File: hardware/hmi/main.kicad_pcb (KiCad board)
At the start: 2 copper layers, 80 x 80 mm, 54 parts, among them J1 LOAD_CON, J2 Conn_01x08, J3 SD_CARD, J4 ENCODER, SW1 CC, SW2 CV, SW3 CR, SW4 CP, SW5 EN, U1 ESP32-DEVKIT-V1

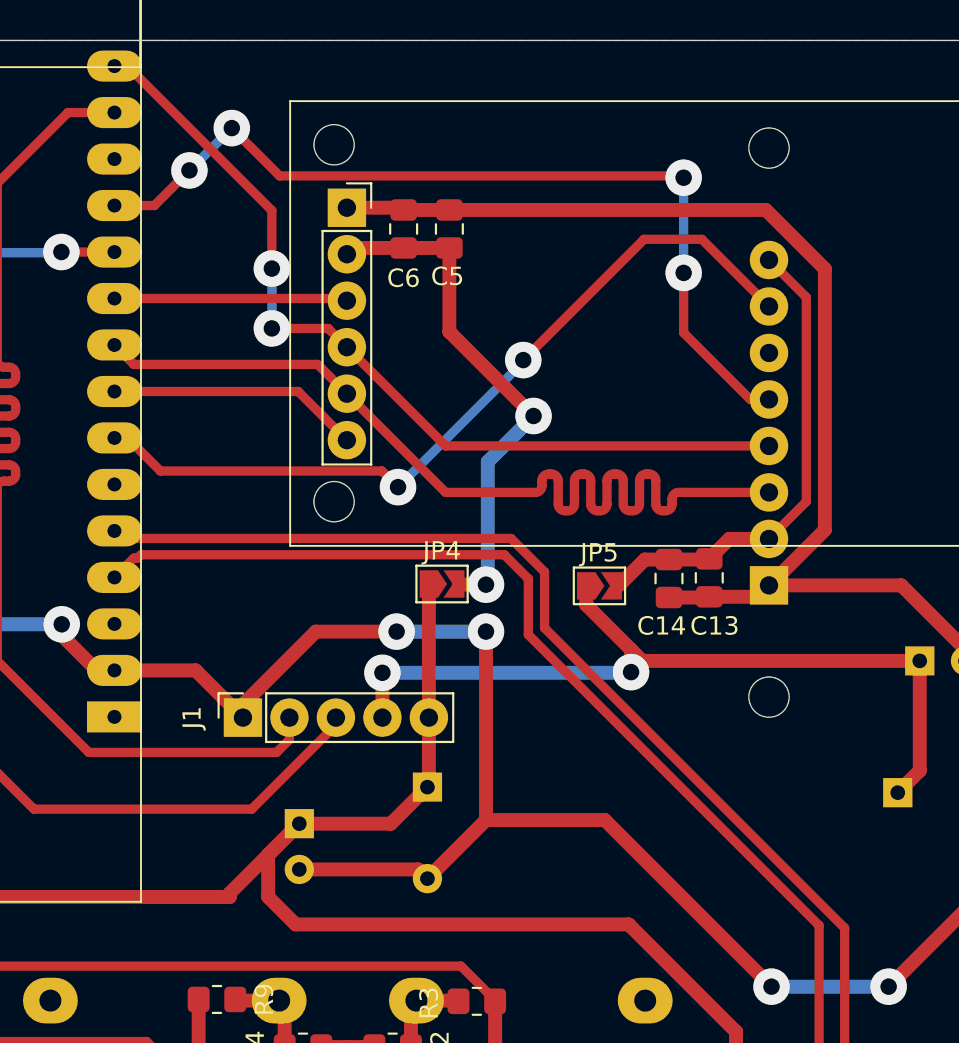
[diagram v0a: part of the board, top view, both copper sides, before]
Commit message: fix: conect DC pin and change reset to avoid conflicts with UART
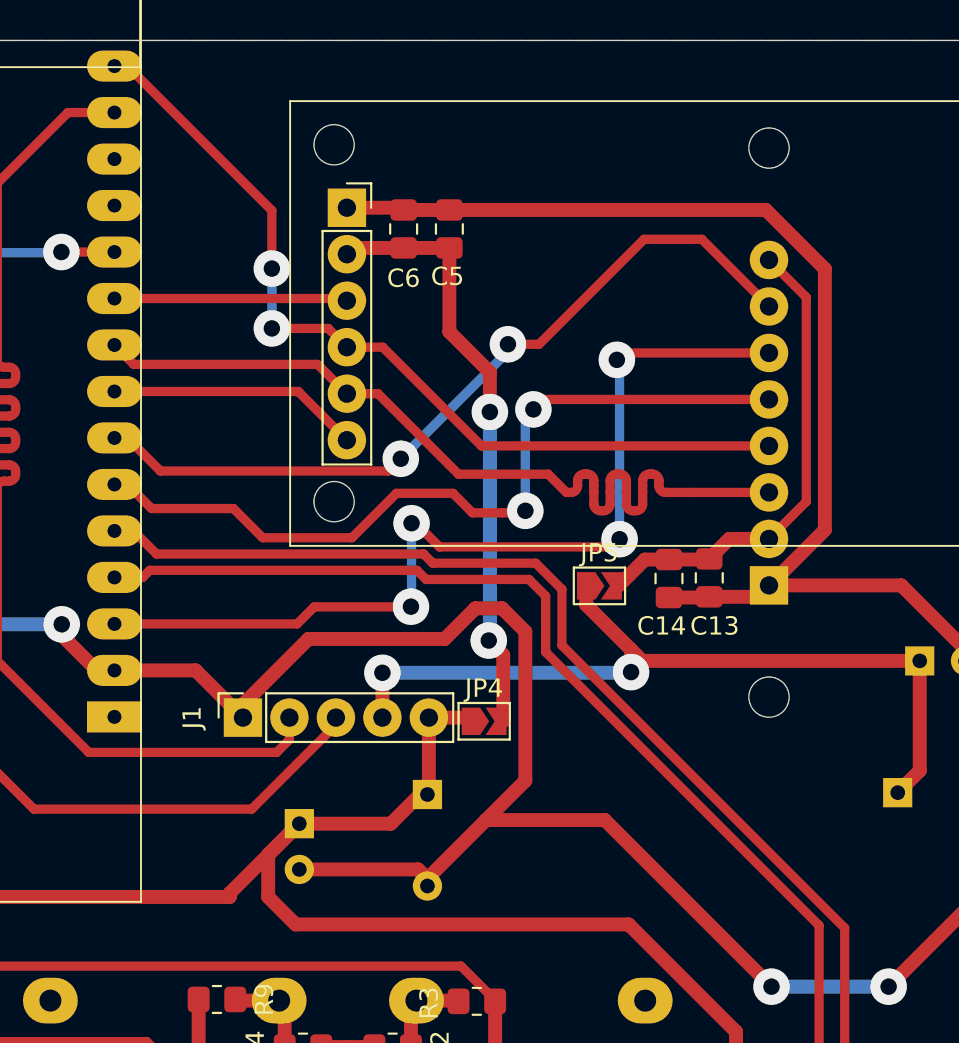
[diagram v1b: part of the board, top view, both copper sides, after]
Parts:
- moved JP4 7.84 mm to (122.5, 96.0)
- moved C1 0.40 mm to (119.4, 100.0)
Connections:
- J2 pad 6: unconnected-(J2-Pin_6-Pad6) -> /DISPLAY/DC
- U1 pad 12: /DISPLAY/RST -> unconnected-(U1-GPIO_3/RX0-Pad12)
- U1 pad 3: unconnected-(U1-GPIO_15_/ADC_13-Pad3) -> /DISPLAY/DC
- U1 pad 6: unconnected-(U1-GPIO_16/RX2-Pad6) -> /DISPLAY/RST
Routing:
- net /DISPLAY/DC: track 0.00 -> 51.6 mm, vias 0 -> 4
- net /DISPLAY/SCK: track 52.1 -> 47.1 mm
- net +5V: track 137.6 -> 132.7 mm
- net /DISPLAY/RST: track 48.6 -> 44.0 mm, vias 4 -> 2
- net Net-(J3-Pin_2): track 28.5 -> 32.9 mm
- net GND: track 377.3 -> 381.4 mm, vias 9 -> 7
- net /ESP32/BTN_EN: track 77.5 -> 76.8 mm
- net /DISPLAY/CS: track 44.1 -> 43.5 mm

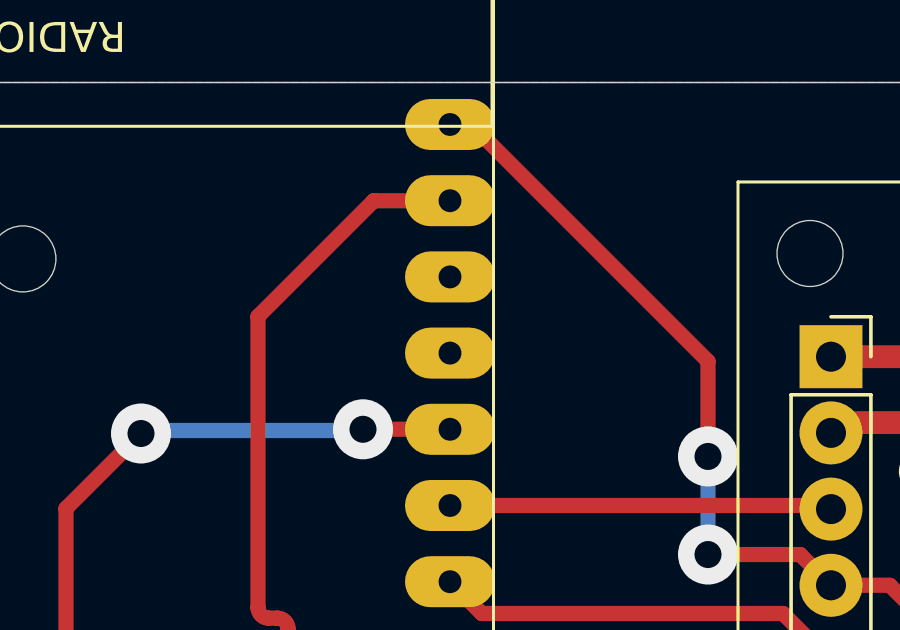
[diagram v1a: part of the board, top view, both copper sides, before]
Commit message: hardware: hmi: Change to UART
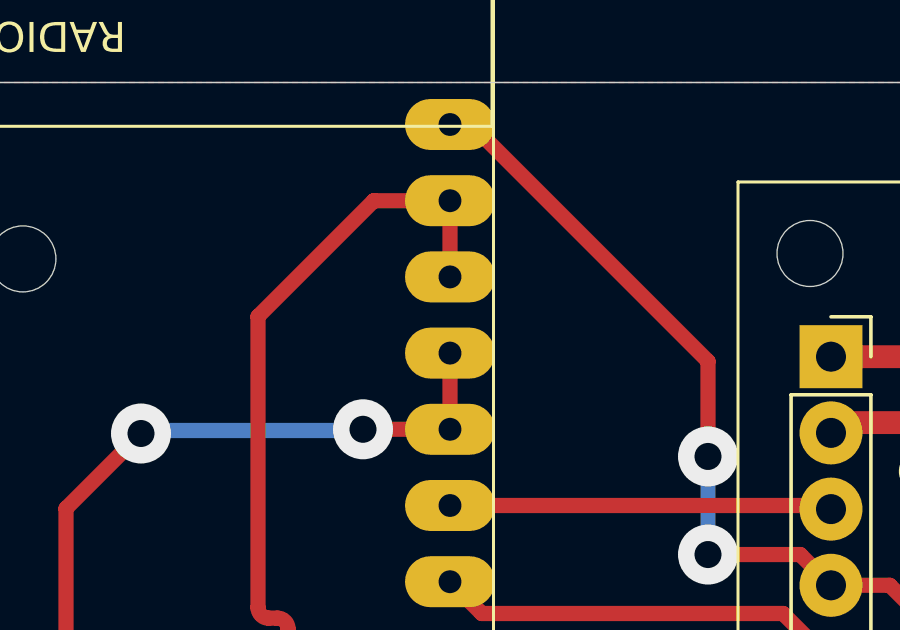
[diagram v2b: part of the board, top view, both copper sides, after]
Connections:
- U1 pad 12: unconnected-(U1-GPIO_3/RX0-Pad12) -> /LOAD_SCL
- U1 pad 13: unconnected-(U1-GPIO_1/TX0-Pad13) -> /LOAD_SDA
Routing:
- net /LOAD_SDA: track 65.0 -> 67.5 mm
- net /LOAD_SCL: track 64.0 -> 66.5 mm
